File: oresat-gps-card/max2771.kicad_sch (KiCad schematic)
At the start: 39 parts, among them U20 D32G-016.368M, U21 MAX2771ETI+, U22 LT1719IS6

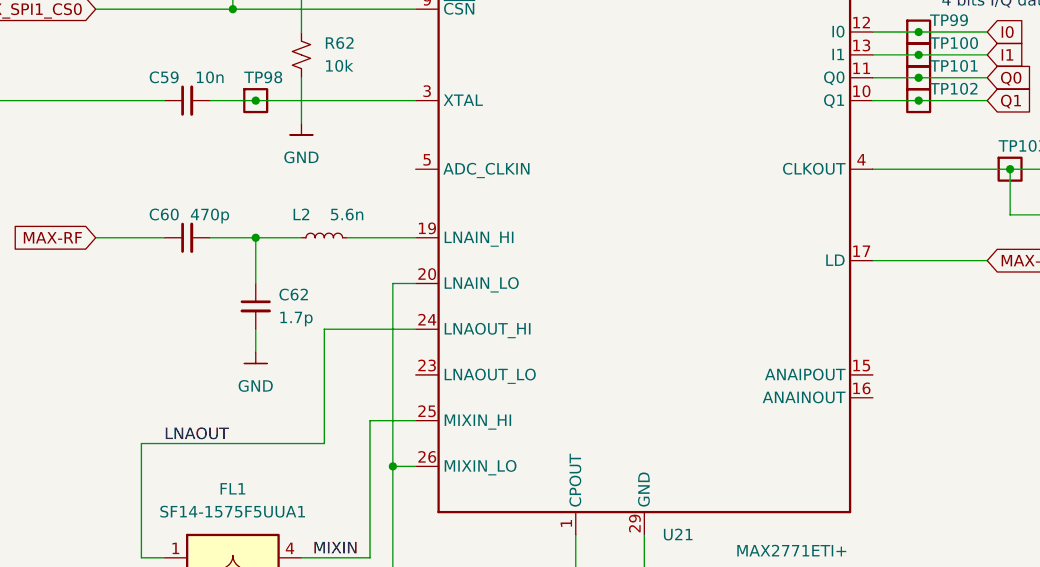
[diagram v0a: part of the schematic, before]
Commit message: GPS card design review changes and issue fixes
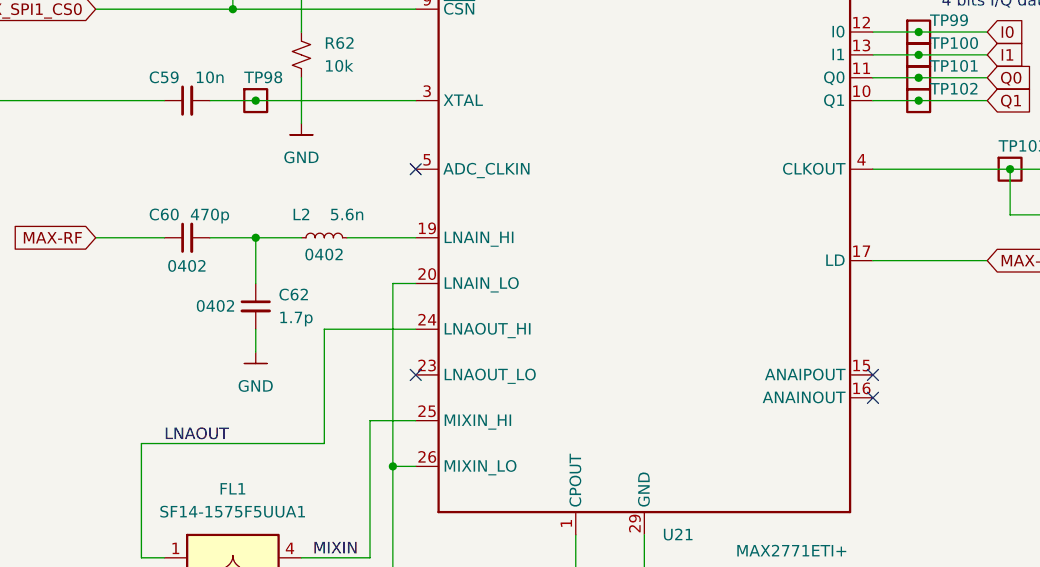
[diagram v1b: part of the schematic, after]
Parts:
- C60, C62, L2: Field4 (none) -> 0402
- C66, C67: footprint Capacitor_SMD:C_0603_1608Metric -> Capacitor_SMD:C_0402_1005Metric
- R63: footprint Resistor_SMD:R_0603_1608Metric -> Resistor_SMD:R_0402_1005Metric
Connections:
- no-connect marks 0 -> 4
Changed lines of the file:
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@@
   (junction (at 180.34 58.42) (diameter 0) (color 0 0 0 0)
   )
+  (no_connect (at 238.76 152.4))
+  (no_connect (at 187.96 129.54))
+  (no_connect (at 187.96 152.4))
+  (no_connect (at 238.76 154.94))
   (wire (pts (xy 152.4 137.16) (xy 160.02 137.16))
     (stroke (width 0) (type default) (color 0 0 0 0))
@@
       (effects (font (size 1.27 1.27)) hide)
     )
+    (property "Field4" "0402" (id 4) (at 162.56 140.335 90))
     (pin "1")
     (pin "2")
@@
     (property "Reference" "R63" (id 0) (at 208.28 195.58 90))
     (property "Value" "20k" (id 1) (at 213.36 195.58 90))
-    (property "Footprint" "Resistor_SMD:R_0603_1608Metric" (id 2) (at 210.82 198.12 0)
+    (property "Footprint" "Resistor_SMD:R_0402_1005Metric" (id 2) (at 210.82 198.12 0)
       (effects (font (size 1.27 1.27)) hide)
     )
@@
     (property "Reference" "C66" (id 0) (at 200.66 204.47 0))
     (property "Value" "27p" (id 1) (at 200.66 201.93 0))
-    (property "Footprint" "Capacitor_SMD:C_0603_1608Metric" (id 2) (at 205.74 203.2 0)
+    (property "Footprint" "Capacitor_SMD:C_0402_1005Metric" (id 2) (at 205.74 203.2 0)
       (effects (font (size 1.27 1.27)) hide)
     )
@@
       (effects (font (size 1.27 1.27)) hide)
     )
+    (property "Field4" "0402" (id 4) (at 177.8 139.065 90))
     (pin "1")
     (pin "2")
@@
   )
   (symbol (lib_id "Device:C_Small") (at 170.18 144.78 0) (unit 1)
-    (in_bom yes) (on_board yes) (fields_autoplaced)
+    (in_bom yes) (on_board yes)
     (property "Reference" "C62" (id 0) (at 172.72 143.5162 0)
       (effects (font (size 1.27 1.27)) (justify left))
@@
       (effects (font (size 1.27 1.27)) hide)
     )
+    (property "Field4" "0402" (id 4) (at 165.735 144.78 0))
     (pin "1")
     (pin "2")
@@
     (property "Reference" "C67" (id 0) (at 220.98 204.47 0))
     (property "Value" "470p" (id 1) (at 220.98 201.93 0))
-    (property "Footprint" "Capacitor_SMD:C_0603_1608Metric" (id 2) (at 215.9 203.2 0)
-      (effects (font (size 1.27 1.27)) hide)
-    )
+    (property "Footprint" "Capacitor_SMD:C_0402_1005Metric" (id 2) (at 215.9 203.2 0)
+      (effects (font (size 1.27 1.27)) hide)
+    )
